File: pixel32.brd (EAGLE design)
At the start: 100 parts, among them CON1 DS1066-07M-SIDE, CON2 DS1066-07M-SIDE, IC1 STM32F030K6TX-LQFP32(7X7), IC108 IRS44273L, IC2 TPS54260, IC208 IRS44273L, IC3 ST3485SOIC8, IC308 IRS44273L, IC4 ESDA6V1L, IC5 3.3, IC6 MC74VHC1GT125, IC7 MC74VHC1GT125, Q101 FDC6420C, Q201 FDC6420C, Q301 FDC6420C

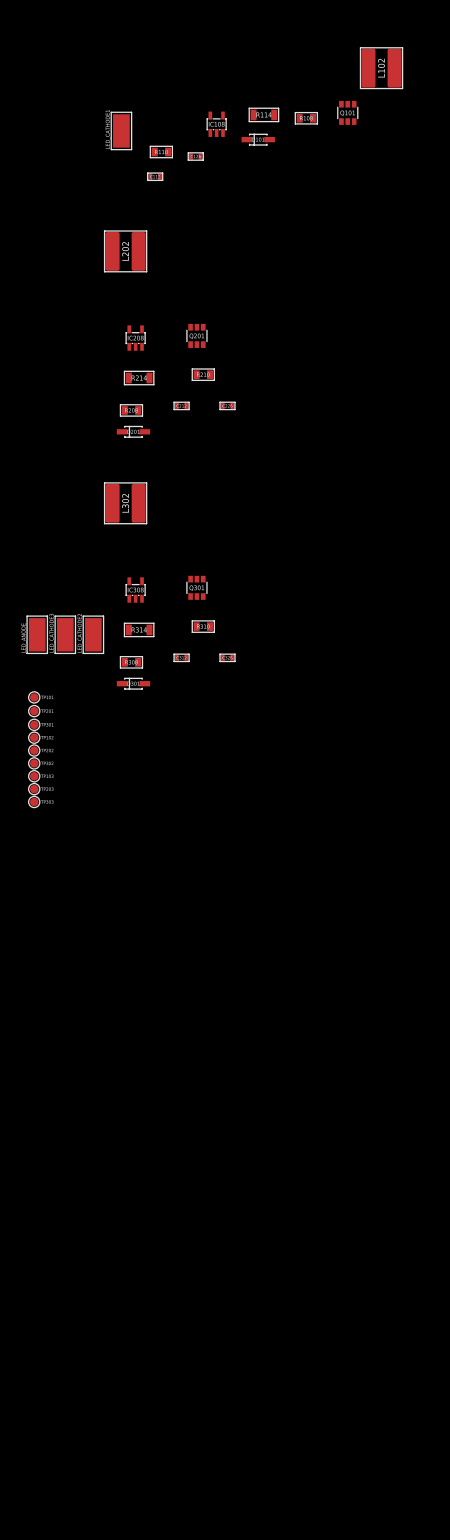
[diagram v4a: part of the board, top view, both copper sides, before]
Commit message: LED driver updated
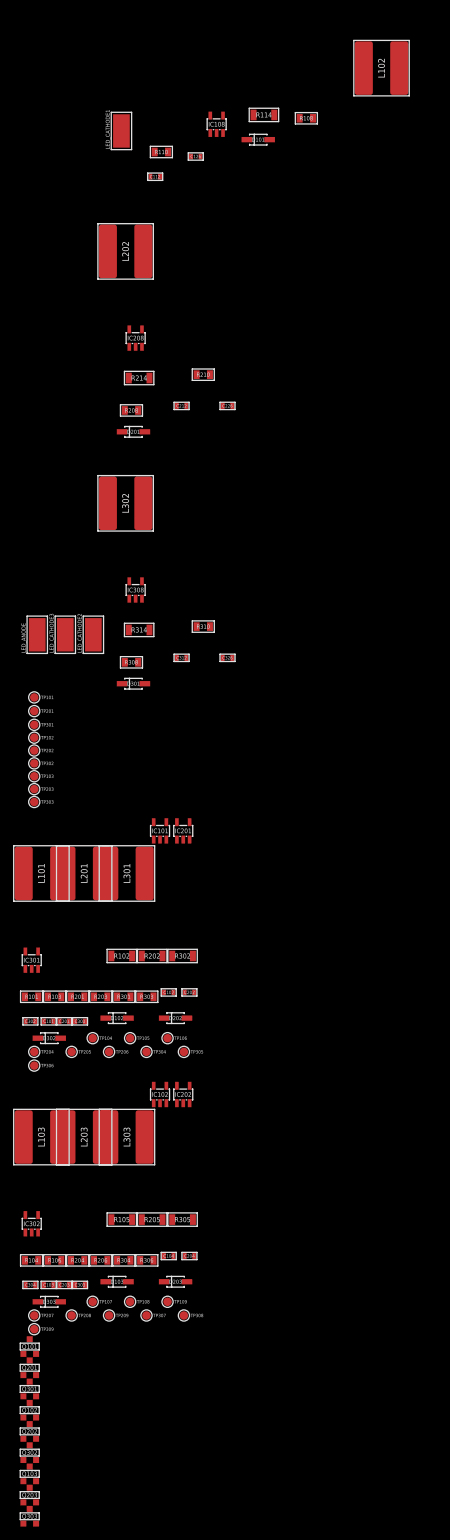
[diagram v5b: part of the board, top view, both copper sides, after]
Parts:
- added C101, C103, C201, C203, C301, C303: 1 uF, rc:C0603
- added C102, C104, C202, C204, C302, C304: 100 nF, rc:C0603
- added D102, D103, D202, D203, D302, D303: CRS08-SOD123, FMU_masterlib:SOD123
- added IC101, IC102, IC201, IC202, IC301, IC302: IRS44273L, pixel_masterlib:SOT23-5
- added L101, L103, L201, L203, L301, L303: 47UH, power_inductors:SDR0805
- added Q102, Q103, Q202, Q203, Q302, Q303: (no value), pixel_masterlib:SOT23
- added R101, R103, R104, R106, R201, R203, R204, R206, R301, R303, R304, R306: 22R, rc:R0805
- added R102, R105, R202, R205, R302, R305: 2R, rc:R1206
- added TP104, TP105, TP106, TP107, TP108, TP109, TP204, TP205, TP206, TP207, TP208, TP209, TP304, TP305, TP306, TP307, TP308, TP309: PAD.05, pixhawk2:PAD.05X.05
- L102, L202, L302: device power_inductors:SDR0604 -> power_inductors:SDR0805
- Q101, Q201, Q301: value FDC6420C -> (none); device pixel_masterlib:SOT23-6 -> pixel_masterlib:SOT23
- moved Q101 190.7 mm to (-84.5, -276.9)
- moved Q201 156.4 mm to (-84.5, -280.1)
- moved Q301 122.5 mm to (-84.5, -283.2)
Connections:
- net N$24 renamed LED_DRIVER3:LED1_PWM
- net N$29 renamed LED_DRIVER2:LED1_PWM
- net N$31 renamed LED_DRIVER1:LED1_PWM
- removed net N$25: C312.2, Q301.5, R314.P$2, TP303.P$1
- removed net N$26: C126.2, C226.2, C326.2, IC108.5, IC208.5, IC308.5
- removed net N$27: C212.2, Q201.5, R214.P$2, TP203.P$1
- removed net N$30: C112.2, Q101.5, R114.P$2, TP103.P$1
- new net LED_DRIVER1:LED1_CATHODE: L102.2
- new net LED_DRIVER1:LED1_CURRENT_SENS: C112.2, Q101.2, R114.P$2, TP103.P$1
- new net LED_DRIVER1:LED2_CATHODE: L101.2
- new net LED_DRIVER1:LED2_CURRENT_SENS: C102.2, Q102.2, R102.P$2, TP106.P$1
- new net LED_DRIVER1:LED2_PWM: IC101.1, R103.1, TP104.P$1
- new net LED_DRIVER1:LED3_CATHODE: L103.2
- new net LED_DRIVER1:LED3_CURRENT_SENS: C104.2, Q103.2, R105.P$2, TP109.P$1
- new net LED_DRIVER1:LED3_PWM: IC102.1, R106.1, TP107.P$1
- new net LED_DRIVER1:LED_COMMON_ANODE: D101.C, D102.C, D103.C
- new net LED_DRIVER1:N$4: Q102.1, R101.2
- new net LED_DRIVER1:N$5: D102.A, L101.1, Q102.3, TP105.P$1
- new net LED_DRIVER1:N$6: IC101.3, IC101.4, R101.1, R103.2
- new net LED_DRIVER1:N$7: Q101.1, R108.2
- new net LED_DRIVER1:N$8: D103.A, L103.1, Q103.3, TP108.P$1
- new net LED_DRIVER1:N$9: IC102.3, IC102.4, R104.1, R106.2
- new net LED_DRIVER1:VDD_12V: C101.2, C103.2, C126.2, IC101.5, IC102.5, IC108.5
- new net LED_DRIVER2:LED1_CATHODE: L202.2
- new net LED_DRIVER2:LED1_CURRENT_SENS: C212.2, Q201.2, R214.P$2, TP203.P$1
- new net LED_DRIVER2:LED2_CATHODE: L201.2
- new net LED_DRIVER2:LED2_CURRENT_SENS: C202.2, Q202.2, R202.P$2, TP206.P$1
- new net LED_DRIVER2:LED2_PWM: IC201.1, R203.1, TP204.P$1
- new net LED_DRIVER2:LED3_CATHODE: L203.2
- new net LED_DRIVER2:LED3_CURRENT_SENS: C204.2, Q203.2, R205.P$2, TP209.P$1
- new net LED_DRIVER2:LED3_PWM: IC202.1, R206.1, TP207.P$1
- new net LED_DRIVER2:LED_COMMON_ANODE: D201.C, D202.C, D203.C
- new net LED_DRIVER2:N$4: Q202.1, R201.2
- new net LED_DRIVER2:N$5: D202.A, L201.1, Q202.3, TP205.P$1
- new net LED_DRIVER2:N$6: IC201.3, IC201.4, R201.1, R203.2
- new net LED_DRIVER2:N$7: Q201.1, R208.2
- new net LED_DRIVER2:N$8: D203.A, L203.1, Q203.3, TP208.P$1
- new net LED_DRIVER2:N$9: IC202.3, IC202.4, R204.1, R206.2
- new net LED_DRIVER2:VDD_12V: C201.2, C203.2, C226.2, IC201.5, IC202.5, IC208.5
- new net LED_DRIVER3:LED1_CATHODE: L302.2
- new net LED_DRIVER3:LED1_CURRENT_SENS: C312.2, Q301.2, R314.P$2, TP303.P$1
- new net LED_DRIVER3:LED2_CATHODE: L301.2
- new net LED_DRIVER3:LED2_CURRENT_SENS: C302.2, Q302.2, R302.P$2, TP306.P$1
- new net LED_DRIVER3:LED2_PWM: IC301.1, R303.1, TP304.P$1
- new net LED_DRIVER3:LED3_CATHODE: L303.2
- new net LED_DRIVER3:LED3_CURRENT_SENS: C304.2, Q303.2, R305.P$2, TP309.P$1
- new net LED_DRIVER3:LED3_PWM: IC302.1, R306.1, TP307.P$1
- new net LED_DRIVER3:LED_COMMON_ANODE: D301.C, D302.C, D303.C
- new net LED_DRIVER3:N$4: Q302.1, R301.2
- new net LED_DRIVER3:N$5: D302.A, L301.1, Q302.3, TP305.P$1
- new net LED_DRIVER3:N$6: IC301.3, IC301.4, R301.1, R303.2
- new net LED_DRIVER3:N$7: Q301.1, R308.2
- new net LED_DRIVER3:N$8: D303.A, L303.1, Q303.3, TP308.P$1
- new net LED_DRIVER3:N$9: IC302.3, IC302.4, R304.1, R306.2
- new net LED_DRIVER3:VDD_12V: C301.2, C303.2, C326.2, IC301.5, IC302.5, IC308.5
- net LED_DRIVER1:N$1: now also Q103.1, R104.2; no longer Q101.1, R108.2
- net LED_DRIVER1:N$2: now also Q101.3; no longer Q101.6
- net LED_DRIVER2:N$1: now also Q203.1, R204.2; no longer Q201.1, R208.2
- net LED_DRIVER2:N$2: now also Q201.3; no longer Q201.6
- net LED_DRIVER3:N$1: now also Q303.1, R304.2; no longer Q301.1, R308.2
- net LED_DRIVER3:N$2: now also Q301.3; no longer Q301.6
- net N$10: no longer L102.2
- net N$20: no longer D101.C, D201.C, D301.C
- net N$21: no longer L202.2
- net N$23: no longer L302.2
- net N$28: now also C101.1, C102.1, C103.1, C104.1, C201.1, C202.1, C203.1, C204.1, C301.1, C302.1, C303.1, C304.1, IC101.2, IC102.2, IC201.2, IC202.2, IC301.2, IC302.2, R102.P$1, R105.P$1, R202.P$1, R205.P$1, R302.P$1, R305.P$1

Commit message: blah
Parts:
- removed C101, C103, C201, C203, C301, C303: 1 uF, rc:C0603
- removed C102, C104, C202, C204, C302, C304: 100 nF, rc:C0603
- removed D102, D103, D202, D203, D302, D303: CRS08-SOD123, FMU_masterlib:SOD123
- removed IC101, IC102, IC201, IC202, IC301, IC302: IRS44273L, pixel_masterlib:SOT23-5
- removed L101, L103, L201, L203, L301, L303: 47UH, power_inductors:SDR0805
- removed Q102, Q103, Q202, Q203, Q302, Q303: (no value), pixel_masterlib:SOT23
- removed R101, R103, R104, R106, R201, R203, R204, R206, R301, R303, R304, R306: 22R, rc:R0805
- removed R102, R105, R202, R205, R302, R305: 2R, rc:R1206
- removed TP104, TP105, TP106, TP107, TP108, TP109, TP204, TP205, TP206, TP207, TP208, TP209, TP304, TP305, TP306, TP307, TP308, TP309: PAD.05, pixhawk2:PAD.05X.05
- added U$2: (no value), pixel_masterlib:BOARD_OUTLINE
- R11, R12: device rc:R0805 -> rc:R0603
- moved Q101 356.5 mm to (46.5, 54.7)
- moved Q201 356.5 mm to (46.5, 51.5)
- moved Q301 356.5 mm to (46.5, 48.3)
- moved LED_ANODE 185.0 mm to (25.0, -20.5)
- moved IC308 181.4 mm to (59.3, -35.1)
- moved R208 181.4 mm to (58.7, -8.22)
- moved TP103 181.4 mm to (44.1, -63.0)
- moved TP201 181.4 mm to (44.1, -53.2)
- moved C112 181.4 mm to (62.2, 26.8)
- moved C126 181.4 mm to (68.3, 29.8)
- moved C212 181.4 mm to (66.2, -7.55)
- moved C226 181.4 mm to (73.0, -7.55)
- moved C312 181.4 mm to (66.2, -45.2)
- moved C326 181.4 mm to (73.0, -45.2)
- moved D101 181.4 mm to (77.7, 32.3)
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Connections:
- net DATA_IN renamed DATA
- net LED_DRIVER1:LED1_CURRENT_SENS renamed N$30
- net LED_DRIVER2:LED1_CURRENT_SENS renamed N$27
- net LED_DRIVER3:LED1_CURRENT_SENS renamed N$25
- removed net DATA_OUT: RN2.1
- removed net LATCH: D4.6, IC1.21, IC7.2, RN1.3
- removed net LATCH_BUFFERED: IC7.4, RN2.3
- removed net LED_DRIVER1:LED1_CATHODE: L102.2
- removed net LED_DRIVER1:LED2_CATHODE: L101.2
- removed net LED_DRIVER1:LED2_CURRENT_SENS: C102.2, Q102.2, R102.P$2, TP106.P$1
- removed net LED_DRIVER1:LED2_PWM: IC101.1, R103.1, TP104.P$1
- removed net LED_DRIVER1:LED3_CATHODE: L103.2
- removed net LED_DRIVER1:LED3_CURRENT_SENS: C104.2, Q103.2, R105.P$2, TP109.P$1
- removed net LED_DRIVER1:LED3_PWM: IC102.1, R106.1, TP107.P$1
- removed net LED_DRIVER1:LED_COMMON_ANODE: D101.C, D102.C, D103.C
- removed net LED_DRIVER1:N$1: Q103.1, R104.2
- removed net LED_DRIVER1:N$4: Q102.1, R101.2
- removed net LED_DRIVER1:N$5: D102.A, L101.1, Q102.3, TP105.P$1
- removed net LED_DRIVER1:N$6: IC101.3, IC101.4, R101.1, R103.2
- removed net LED_DRIVER1:N$8: D103.A, L103.1, Q103.3, TP108.P$1
- removed net LED_DRIVER1:N$9: IC102.3, IC102.4, R104.1, R106.2
- removed net LED_DRIVER2:LED1_CATHODE: L202.2
- removed net LED_DRIVER2:LED2_CATHODE: L201.2
- removed net LED_DRIVER2:LED2_CURRENT_SENS: C202.2, Q202.2, R202.P$2, TP206.P$1
- removed net LED_DRIVER2:LED2_PWM: IC201.1, R203.1, TP204.P$1
- removed net LED_DRIVER2:LED3_CATHODE: L203.2
- removed net LED_DRIVER2:LED3_CURRENT_SENS: C204.2, Q203.2, R205.P$2, TP209.P$1
- removed net LED_DRIVER2:LED3_PWM: IC202.1, R206.1, TP207.P$1
- removed net LED_DRIVER2:LED_COMMON_ANODE: D201.C, D202.C, D203.C
- removed net LED_DRIVER2:N$1: Q203.1, R204.2
- removed net LED_DRIVER2:N$4: Q202.1, R201.2
- removed net LED_DRIVER2:N$5: D202.A, L201.1, Q202.3, TP205.P$1
- removed net LED_DRIVER2:N$6: IC201.3, IC201.4, R201.1, R203.2
- removed net LED_DRIVER2:N$8: D203.A, L203.1, Q203.3, TP208.P$1
- removed net LED_DRIVER2:N$9: IC202.3, IC202.4, R204.1, R206.2
- removed net LED_DRIVER3:LED1_CATHODE: L302.2
- removed net LED_DRIVER3:LED2_CATHODE: L301.2
- removed net LED_DRIVER3:LED2_CURRENT_SENS: C302.2, Q302.2, R302.P$2, TP306.P$1
- removed net LED_DRIVER3:LED2_PWM: IC301.1, R303.1, TP304.P$1
- removed net LED_DRIVER3:LED3_CATHODE: L303.2
- removed net LED_DRIVER3:LED3_CURRENT_SENS: C304.2, Q303.2, R305.P$2, TP309.P$1
- removed net LED_DRIVER3:LED3_PWM: IC302.1, R306.1, TP307.P$1
- removed net LED_DRIVER3:LED_COMMON_ANODE: D301.C, D302.C, D303.C
- removed net LED_DRIVER3:N$1: Q303.1, R304.2
- removed net LED_DRIVER3:N$4: Q302.1, R301.2
- removed net LED_DRIVER3:N$5: D302.A, L301.1, Q302.3, TP305.P$1
- removed net LED_DRIVER3:N$6: IC301.3, IC301.4, R301.1, R303.2
- removed net LED_DRIVER3:N$8: D303.A, L303.1, Q303.3, TP308.P$1
- removed net LED_DRIVER3:N$9: IC302.3, IC302.4, R304.1, R306.2
- removed net MOSI: IC1.28, NRF24L01.6
- removed net SCK: IC1.26, NRF24L01.5
- new net CS: D4.6, IC1.25, RN1.3
- new net CS_OUT: IC1.29, RN2.3
- new net DATA_BUFFERED: IC7.4, RN2.1
- new net MOSI/DATA: IC1.28, IC7.2, NRF24L01.6
- net A: no longer R11.2
- net B: no longer R12.2
- net CLOCK: now also IC1.26, NRF24L01.5; no longer IC1.22
- net LED_DRIVER1:VDD_12V: no longer C101.2, C103.2, IC101.5, IC102.5
- net LED_DRIVER2:VDD_12V: no longer C201.2, C203.2, IC201.5, IC202.5
- net LED_DRIVER3:VDD_12V: no longer C301.2, C303.2, IC301.5, IC302.5
- net N$10: now also L102.2
- net N$20: now also D101.C, D201.C, D301.C
- net N$21: now also L202.2
- net N$23: now also L302.2
- net N$28: no longer C101.1, C102.1, C103.1, C104.1, C201.1, C202.1, C203.1, C204.1, C301.1, C302.1, C303.1, C304.1, IC101.2, IC102.2, IC201.2, IC202.2, IC301.2, IC302.2, R102.P$1, R105.P$1, R202.P$1, R205.P$1, R302.P$1, R305.P$1
- net RS485_A: now also R11.2
- net RS485_B: now also R12.2
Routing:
- net VDD_12V: track 15.7 -> 12.6 mm
- net VDD_3V3: track 1.51 -> 0.00 mm
- net GND: vias 30 -> 28
- added copper zone on layer 1, net GND
- added copper zone on layer 1, net VDD_12V
- added copper zone on layer 1, net VDD_24V
- removed copper zone on layer 1, net N$3
- removed copper zone on layer 1, net VBAT
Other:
- board text added: "Board should not be bigger than 50x50mm and no more than 2 layers"

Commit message: pcb attmepts
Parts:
- removed C112, C18, C212: 100 nF, rc:C0603
- removed IC108, IC208, IC308: IRS44273L, pixel_masterlib:SOT23-5
- removed R108, R110, R208, R210, R308, R310: 22R, rc:R0805
- removed R114, R214, R314: 2R, rc:R1206
- added C101, C103, C201, C203, C26, C301: 100 nF, rc:C0603
- added CON3: PINHEAD_1X02-2.54, pinhead:1X02-PTH-2.54
- added IC101, IC201, IC301: IRS44273L, pixel_masterlib:SOT23-5
- added R101, R103, R201, R203, R301, R303: 22R, rc:R0603
- added R102, R202, R302: 2R, rc:R1206
- added R8: 10K, rc:R0603
- moved C17 111.9 mm to (14.0, -21.5), turned to 180 degrees
- moved C13 98.2 mm to (0.50, -10.5)
- moved C23 97.7 mm to (10.5, -7.00), turned to 180 degrees
- moved D101 97.5 mm to (-14.0, -1.00), turned to 90 degrees
- moved TP101 86.9 mm to (-16.0, 11.5), flipped to the bottom, turned to 90 degrees
- moved C16 84.2 mm to (14.0, -23.0), turned to 180 degrees
- moved Q101 79.3 mm to (-11.0, 0.00), turned to 90 degrees
- moved Q201 68.0 mm to (2.00, 0.00), turned to 90 degrees
- moved C15 67.8 mm to (0.00, -21.5), turned to 90 degrees
- moved C24 67.2 mm to (-14.0, -35.5), turned to 90 degrees
- moved C14 64.7 mm to (1.50, -21.5), turned to 90 degrees
- moved D301 63.1 mm to (22.0, 2.00), turned to 90 degrees
- moved D201 60.4 mm to (-0.50, -1.00), turned to 90 degrees
- moved Q301 57.9 mm to (14.5, 0.00), turned to 90 degrees
- moved LED_ANODE 57.2 mm to (-21.0, 13.5)
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- renumbered C126 to C102, C226 to C202, C312 to C303, C326 to C302
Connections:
- removed net N$20: D101.C, D201.C, D301.C, LED_ANODE.1
- net GND: now also C19.2, C26.1, R8.1; no longer C18.1, C19.1
- net LED_DRIVER1:LED1_PWM: now also IC101.1, R103.1; no longer IC108.1, R110.1
- net LED_DRIVER1:N$3: now also IC101.3, IC101.4, R101.1, R103.2; no longer IC108.3, IC108.4, R108.1, R110.2
- net LED_DRIVER1:N$7: now also R101.2; no longer R108.2
- net LED_DRIVER1:VDD_12V: now also IC101.5; no longer IC108.5
- net LED_DRIVER2:LED1_PWM: now also IC201.1, R203.1; no longer IC208.1, R210.1
- net LED_DRIVER2:N$3: now also IC201.3, IC201.4, R201.1, R203.2; no longer IC208.3, IC208.4, R208.1, R210.2
- net LED_DRIVER2:N$7: now also R201.2; no longer R208.2
- net LED_DRIVER2:VDD_12V: now also IC201.5; no longer IC208.5
- net LED_DRIVER3:LED1_PWM: now also IC301.1, R303.1; no longer IC308.1, R310.1
- net LED_DRIVER3:N$3: now also IC301.3, IC301.4, R301.1, R303.2; no longer IC308.3, IC308.4, R308.1, R310.2
- net LED_DRIVER3:N$7: now also R301.2; no longer R308.2
- net LED_DRIVER3:VDD_12V: now also IC301.5; no longer IC308.5
- net N$10: now also C101.2
- net N$21: now also C201.2
- net N$23: now also C301.2
- net N$25: now also C301.1, R302.P$2; no longer R314.P$2
- net N$27: now also C201.1, C203.2, R202.P$2; no longer C212.2, R214.P$2
- net N$28: now also C103.1, C203.1, IC101.2, IC201.2, IC301.2, R102.P$1, R202.P$1, R302.P$1; no longer C112.1, C212.1, IC108.2, IC208.2, IC308.2, R114.P$1, R214.P$1, R314.P$1
- net N$30: now also C101.1, C103.2, R102.P$2; no longer C112.2, R114.P$2
- net N$4: now also C19.1; no longer C19.2
- net TEMP: now also C26.2, CON3.1, R8.2
- net VDD_12V: now also D101.C, D201.C, D301.C, LED_ANODE.1
- net VDD_3V3: now also CON3.2; no longer C18.2

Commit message: -blah
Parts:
- removed LED3: LED-0603, rc:LED0603
- removed R40: 1K, rc:R0603
- moved IC3 88.4 mm to (48.0, -0.50)
- moved LED2 71.5 mm to (1.50, -18.1)
- moved R39 71.5 mm to (1.50, -19.4)
- moved D4 62.4 mm to (34.0, 19.5)
- moved TP102 56.4 mm to (-17.3, 24.1)
- moved RN1 54.3 mm to (32.5, 12.0)
- moved TP202 52.9 mm to (-6.88, 22.6)
- moved TP301 52.6 mm to (9.28, 22.1)
- moved TP302 51.5 mm to (6.55, 22.1)
- moved TP201 44.9 mm to (-1.00, 22.0), flipped to the top
- moved CON1 34.7 mm to (17.0, 8.00), turned to 270 degrees
- moved RN2 30.6 mm to (43.5, -16.5)
- moved C23 25.5 mm to (36.0, -5.50), turned to 270 degrees
- moved IC6 22.9 mm to (33.0, -5.50), turned to 90 degrees
- moved C16 22.2 mm to (2.50, -4.00), turned to 270 degrees
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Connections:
- removed net CK: IC1.10
- removed net DC-DC_FB: IC1.6
- removed net DC-DC_PWM: IC1.13
- removed net LED2: R40.2
- removed net LED2_FB: IC1.11
- removed net LED3_FB: IC1.12
- removed net LED_DRIVER1:LED1_PWM: IC101.1, R103.1, TP101.P$1
- removed net LED_DRIVER2:LED1_PWM: IC201.1, R203.1, TP201.P$1
- removed net LED_DRIVER3:LED1_PWM: IC301.1, R303.1, TP301.P$1
- removed net N$1: LED3.A, R40.1
- removed net N$25: C301.1, C303.2, Q301.2, R302.P$2, TP303.P$1
- removed net N$27: C201.1, C203.2, Q201.2, R202.P$2, TP203.P$1
- removed net N$30: C101.1, C103.2, Q101.2, R102.P$2, TP103.P$1
- new net LED1_CURRENT: C101.1, C103.2, IC1.10, Q101.2, R102.P$2, TP103.P$1
- new net LED2_CURRENT: C201.1, C203.2, IC1.11, Q201.2, R202.P$2, TP203.P$1
- new net LED3_CURRENT: C301.1, C303.2, IC1.12, Q301.2, R302.P$2, TP303.P$1
- net GND: no longer LED3.C
- net LED1_PWM: now also IC101.1, R103.1, TP101.P$1
- net LED2_PWM: now also IC201.1, R203.1, TP201.P$1
- net LED3_PWM: now also IC301.1, R303.1, TP301.P$1
